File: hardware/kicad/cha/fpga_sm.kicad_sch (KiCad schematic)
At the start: 31 parts, among them J3 PROG SM, U15 iCE40HX4K-TQ144, U16 W25Q32JVSS, X2 25 MHz 3,3 V

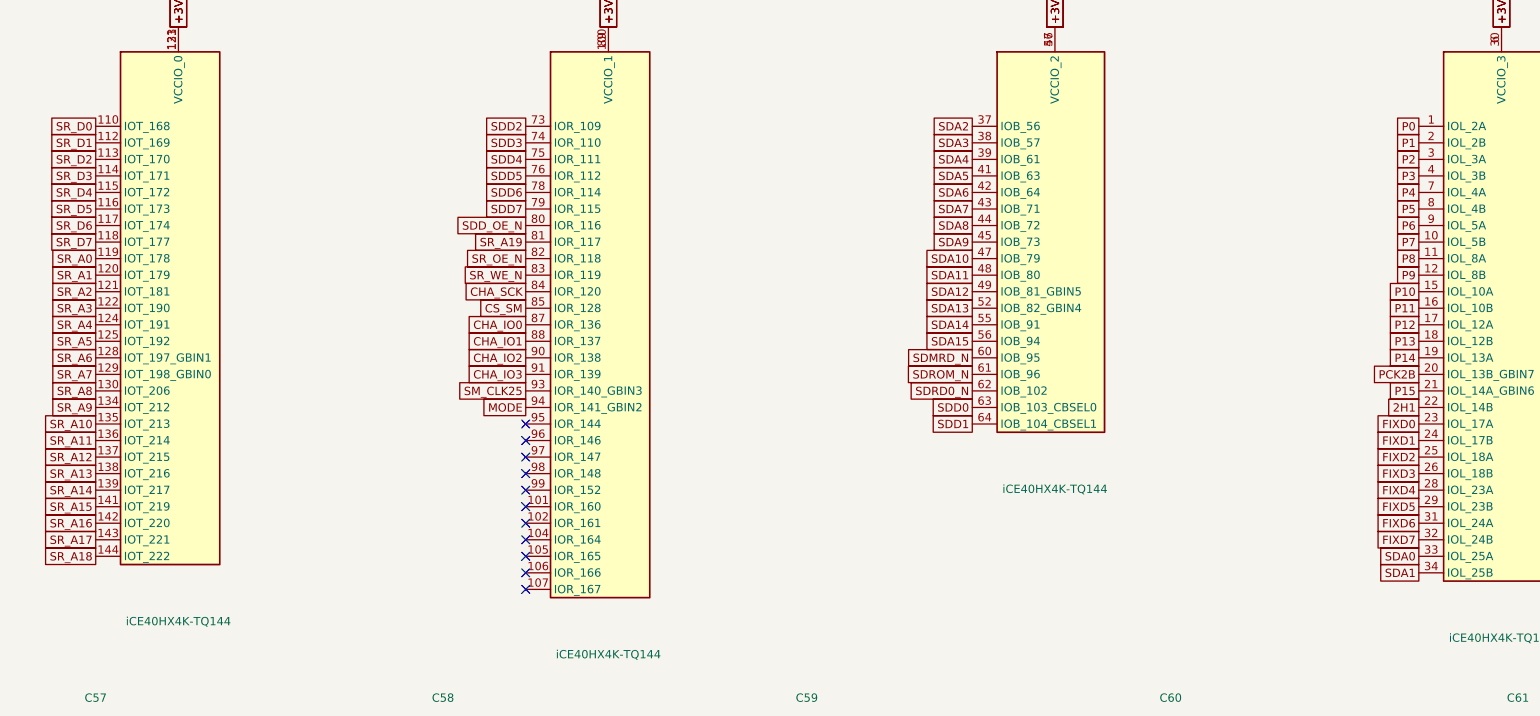
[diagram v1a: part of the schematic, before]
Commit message: Circuits imprimés 2 couches : placement et affectation des broches FPGA
- hardware/gen/pcb.py : empreintes et réseaux depuis boards.py, contour
  depuis outline.py ; ancres placées (contacts, rangée de tampons, FPGA,
  mémoires ; CHA : Pico au centre, microSD et bouton en haut), passifs
  au plus près de leur broche, masse coulée sur les deux faces.
- --pins : signaux des FPGA affectés aux broches tournées vers leur
  cible en conservant l'ordre circulaire (pins_opt.json, repris par
  fpga_pins.py) ; stable en trois passes.
- boards.py : canaux des tampons triés selon la position des contacts.
- hardware/gen/route.py : export Specctra, Freerouting, relecture de la
  session, DRC.
Placement-routage FPGA avec les nouvelles broches : en cours de
vérification.

Co-Authored-By: Claude Opus 5.5 <noreply@anthropic.com>
Claude-Session: https://claude.ai/code/session_01WKfXP1YJ8otGxZ5dsY6Agh
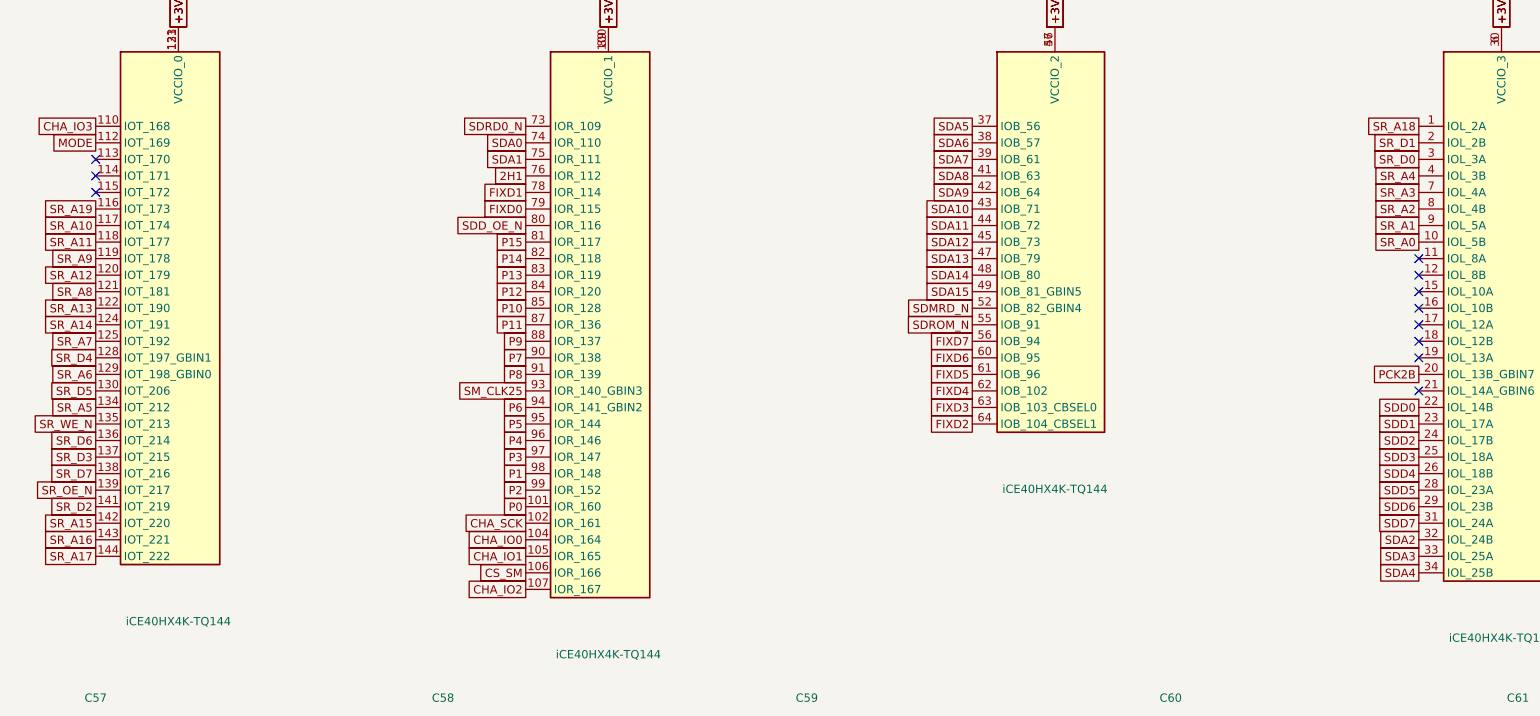
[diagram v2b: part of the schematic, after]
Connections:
- net 2H1: now also U15.76 (IOR_112); no longer U15.22 (IOL_14B)
- net CHA_IO0: now also U15.104 (IOR_164); no longer U15.87 (IOR_136)
- net CHA_IO1: now also U15.105 (IOR_165); no longer U15.88 (IOR_137)
- net CHA_IO2: now also U15.107 (IOR_167); no longer U15.90 (IOR_138)
- net CHA_IO3: now also U15.110 (IOT_168); no longer U15.91 (IOR_139)
- net CHA_SCK: now also U15.102 (IOR_161); no longer U15.84 (IOR_120)
- net CS_SM: now also U15.106 (IOR_166); no longer U15.85 (IOR_128)
- net FIXD0: now also U15.79 (IOR_115); no longer U15.23 (IOL_17A)
- net FIXD1: now also U15.78 (IOR_114); no longer U15.24 (IOL_17B)
- net FIXD2: now also U15.64 (IOB_104_CBSEL1); no longer U15.25 (IOL_18A)
- net FIXD3: now also U15.63 (IOB_103_CBSEL0); no longer U15.26 (IOL_18B)
- net FIXD4: now also U15.62 (IOB_102); no longer U15.28 (IOL_23A)
- net FIXD5: now also U15.61 (IOB_96); no longer U15.29 (IOL_23B)
- net FIXD6: now also U15.60 (IOB_95); no longer U15.31 (IOL_24A)
- net FIXD7: now also U15.56 (IOB_94); no longer U15.32 (IOL_24B)
- net MODE: now also U15.112 (IOT_169); no longer U15.94 (IOR_141_GBIN2)
- net P0: now also U15.101 (IOR_160); no longer U15.1 (IOL_2A)
- net P1: now also U15.98 (IOR_148); no longer U15.2 (IOL_2B)
- net P10: now also U15.85 (IOR_128); no longer U15.15 (IOL_10A)
- net P11: now also U15.87 (IOR_136); no longer U15.16 (IOL_10B)
- net P12: now also U15.84 (IOR_120); no longer U15.17 (IOL_12A)
- net P13: now also U15.83 (IOR_119); no longer U15.18 (IOL_12B)
- net P14: now also U15.82 (IOR_118); no longer U15.19 (IOL_13A)
- net P15: now also U15.81 (IOR_117); no longer U15.21 (IOL_14A_GBIN6)
- net P2: now also U15.99 (IOR_152); no longer U15.3 (IOL_3A)
- net P3: now also U15.97 (IOR_147); no longer U15.4 (IOL_3B)
- net P4: now also U15.96 (IOR_146); no longer U15.7 (IOL_4A)
- net P5: now also U15.95 (IOR_144); no longer U15.8 (IOL_4B)
- net P6: now also U15.94 (IOR_141_GBIN2); no longer U15.9 (IOL_5A)
- net P7: now also U15.90 (IOR_138); no longer U15.10 (IOL_5B)
- net P8: now also U15.91 (IOR_139); no longer U15.11 (IOL_8A)
- net P9: now also U15.88 (IOR_137); no longer U15.12 (IOL_8B)
- net SDA0: now also U15.74 (IOR_110); no longer U15.33 (IOL_25A)
- net SDA1: now also U15.75 (IOR_111); no longer U15.34 (IOL_25B)
- net SDA10: now also U15.43 (IOB_71); no longer U15.47 (IOB_79)
- net SDA11: now also U15.44 (IOB_72); no longer U15.48 (IOB_80)
- net SDA12: now also U15.45 (IOB_73); no longer U15.49 (IOB_81_GBIN5)
- net SDA13: now also U15.47 (IOB_79); no longer U15.52 (IOB_82_GBIN4)
- net SDA14: now also U15.48 (IOB_80); no longer U15.55 (IOB_91)
- net SDA15: now also U15.49 (IOB_81_GBIN5); no longer U15.56 (IOB_94)
- net SDA2: now also U15.32 (IOL_24B); no longer U15.37 (IOB_56)
- net SDA3: now also U15.33 (IOL_25A); no longer U15.38 (IOB_57)
- net SDA4: now also U15.34 (IOL_25B); no longer U15.39 (IOB_61)
- net SDA5: now also U15.37 (IOB_56); no longer U15.41 (IOB_63)
- net SDA6: now also U15.38 (IOB_57); no longer U15.42 (IOB_64)
- net SDA7: now also U15.39 (IOB_61); no longer U15.43 (IOB_71)
- net SDA8: now also U15.41 (IOB_63); no longer U15.44 (IOB_72)
- net SDA9: now also U15.42 (IOB_64); no longer U15.45 (IOB_73)
- net SDD0: now also U15.22 (IOL_14B); no longer U15.63 (IOB_103_CBSEL0)
- net SDD1: now also U15.23 (IOL_17A); no longer U15.64 (IOB_104_CBSEL1)
- net SDD2: now also U15.24 (IOL_17B); no longer U15.73 (IOR_109)
- net SDD3: now also U15.25 (IOL_18A); no longer U15.74 (IOR_110)
- net SDD4: now also U15.26 (IOL_18B); no longer U15.75 (IOR_111)
- net SDD5: now also U15.28 (IOL_23A); no longer U15.76 (IOR_112)
- net SDD6: now also U15.29 (IOL_23B); no longer U15.78 (IOR_114)
- net SDD7: now also U15.31 (IOL_24A); no longer U15.79 (IOR_115)
- net SDMRD_N: now also U15.52 (IOB_82_GBIN4); no longer U15.60 (IOB_95)
- net SDRD0_N: now also U15.73 (IOR_109); no longer U15.62 (IOB_102)
- net SDROM_N: now also U15.55 (IOB_91); no longer U15.61 (IOB_96)
- net SR_A0: now also U15.10 (IOL_5B); no longer U15.119 (IOT_178)
- net SR_A1: now also U15.9 (IOL_5A); no longer U15.120 (IOT_179)
- net SR_A10: now also U15.117 (IOT_174); no longer U15.135 (IOT_213)
- net SR_A11: now also U15.118 (IOT_177); no longer U15.136 (IOT_214)
- net SR_A12: now also U15.120 (IOT_179); no longer U15.137 (IOT_215)
- net SR_A13: now also U15.122 (IOT_190); no longer U15.138 (IOT_216)
- net SR_A14: now also U15.124 (IOT_191); no longer U15.139 (IOT_217)
- net SR_A15: now also U15.142 (IOT_220); no longer U15.141 (IOT_219)
- net SR_A16: now also U15.143 (IOT_221); no longer U15.142 (IOT_220)
- net SR_A17: now also U15.144 (IOT_222); no longer U15.143 (IOT_221)
- net SR_A18: now also U15.1 (IOL_2A); no longer U15.144 (IOT_222)
- net SR_A19: now also U15.116 (IOT_173); no longer U15.81 (IOR_117)
- net SR_A2: now also U15.8 (IOL_4B); no longer U15.121 (IOT_181)
- net SR_A3: now also U15.7 (IOL_4A); no longer U15.122 (IOT_190)
- net SR_A4: now also U15.4 (IOL_3B); no longer U15.124 (IOT_191)
- net SR_A5: now also U15.134 (IOT_212); no longer U15.125 (IOT_192)
- net SR_A6: now also U15.129 (IOT_198_GBIN0); no longer U15.128 (IOT_197_GBIN1)
- net SR_A7: now also U15.125 (IOT_192); no longer U15.129 (IOT_198_GBIN0)
- net SR_A8: now also U15.121 (IOT_181); no longer U15.130 (IOT_206)
- net SR_A9: now also U15.119 (IOT_178); no longer U15.134 (IOT_212)
- net SR_D0: now also U15.3 (IOL_3A); no longer U15.110 (IOT_168)
- net SR_D1: now also U15.2 (IOL_2B); no longer U15.112 (IOT_169)
- net SR_D2: now also U15.141 (IOT_219); no longer U15.113 (IOT_170)
- net SR_D3: now also U15.137 (IOT_215); no longer U15.114 (IOT_171)
- net SR_D4: now also U15.128 (IOT_197_GBIN1); no longer U15.115 (IOT_172)
- net SR_D5: now also U15.130 (IOT_206); no longer U15.116 (IOT_173)
- net SR_D6: now also U15.136 (IOT_214); no longer U15.117 (IOT_174)
- net SR_D7: now also U15.138 (IOT_216); no longer U15.118 (IOT_177)
- net SR_OE_N: now also U15.139 (IOT_217); no longer U15.82 (IOR_118)
- net SR_WE_N: now also U15.135 (IOT_213); no longer U15.83 (IOR_119)

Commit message: FPGA configurés par le RP2350 depuis la carte SD (plus de flash)
- Matériel : flash SPI retirées (4 W25Q32, 12 résistances, 4
  condensateurs). Le bus de liaison arrive sur les broches de
  configuration des iCE40 (LK_SCK -> 70 SCK, LK_IO[0] -> 68 SDI,
  LK_CS_N -> 71 SS), qui redeviennent ces entrées après le démarrage.
  CRESET_N commun aux 4 FPGA, tiré à la masse, piloté par le RP2350
  (GP28) ; câble PROG-CHA en 2 x 7 (CRESET_N + masse). Connecteur 2 x 3
  de secours par FPGA (iceprog -S).
- Firmware : fpga_boot.c (reset commun en mode SPI esclave, envoi des
  SDAES/fpga_*.bin l'un après l'autre, contrôle de CDONE) ; testé sur
  PC (bitstreams reçus à l'identique, FPGA laissés en reset si un
  fichier manque).
- make -C hdl sd : fichiers à copier sur la carte SD.
- PCB : table de placement et références des FPGA mises à jour,
  broches réoptimisées.
Placement-routage des FPGA avec les nouvelles broches : en cours.

Co-Authored-By: Claude Opus 5.5 <noreply@anthropic.com>
Claude-Session: https://claude.ai/code/session_01WKfXP1YJ8otGxZ5dsY6Agh
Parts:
- removed C70, C71: 100n, Capacitor_SMD:C_0603_1608Metric, symbol Device:C
- removed R13, R14: 100, Resistor_SMD:R_0603_1608Metric, symbol Device:R
- removed R15, R16, R17, R18: 10k, Resistor_SMD:R_0603_1608Metric, symbol Device:R
- removed U15: iCE40HX4K-TQ144, Package_QFP:TQFP-144_20x20mm_P0.5mm, symbol FPGA_Lattice:ICE40HX4K-TQ144
- removed U16: W25Q32JVSS, Package_SO:SOIC-8_5.23x5.23mm_P1.27mm, symbol Memory_Flash:W25Q32JVSS
- added C50: 100n, Capacitor_SMD:C_0603_1608Metric, symbol Device:C
- added R10, R11: 100, Resistor_SMD:R_0603_1608Metric, symbol Device:R
- added R12: 10k, Resistor_SMD:R_0603_1608Metric, symbol Device:R
- added U14: iCE40HX4K-TQ144, Package_QFP:TQFP-144_20x20mm_P0.5mm, symbol FPGA_Lattice:ICE40HX4K-TQ144
- C54, C64, C67: value 100n -> 10u; footprint Capacitor_SMD:C_0603_1608Metric -> Capacitor_SMD:C_0805_2012Metric
- C55, C66, C68: value 10u -> 100n; footprint Capacitor_SMD:C_0805_2012Metric -> Capacitor_SMD:C_0603_1608Metric
- J3: value PROG SM -> CONF SM
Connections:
- net SM_FL_CS_N is gone; now on net CS_SM: J3.2 (Pin_2)
- net SM_FL_DO is gone; now on net CHA_IO0: J3.4 (Pin_4)
- net SM_FL_SCK is gone; now on net CHA_SCK: J3.1 (Pin_1)
- net +1V2: now also C50.1, R10.1, R11.1, U14.111 (VCC), U14.27 (VCC), U14.40 (VCC), U14.92 (VCC); no longer C55.1
- net +3V3: now also C55.1, C69.1, U14.100 (VCCIO_1), U14.108 (VPP_2V5), U14.123 (VCCIO_0), U14.131 (VCCIO_0), U14.30 (VCCIO_3), U14.46 (VCCIO_2), U14.57 (VCCIO_2), U14.6 (VCCIO_3), U14.72 (VCC_SPI), U14.89 (VCCIO_1); no longer C65.1
- net 2H1: now also U14.78 (IOR_114)
- net CDONE: now also U14.65 (CDONE)
- net CHA_IO0: now also U14.68 (IOB_106_SDI)
- net CHA_IO1: now also U14.104 (IOR_164)
- net CHA_IO2: now also U14.105 (IOR_165)
- net CHA_IO3: now also U14.106 (IOR_166)
- net CHA_SCK: now also U14.70 (IOB_107_SCK)
- net CS_SM: now also U14.71 (IOB_108_SS)
- net FIXD0: now also U14.80 (IOR_116)
- net FIXD1: now also U14.79 (IOR_115)
- net FIXD2: now also U14.73 (IOR_109)
- net FIXD3: now also U14.64 (IOB_104_CBSEL1)
- net FIXD4: now also U14.63 (IOB_103_CBSEL0)
- net FIXD5: now also U14.62 (IOB_102)
- net FIXD6: now also U14.61 (IOB_96)
- net FIXD7: now also U14.60 (IOB_95)
- net GND: now also C50.2, R12.2, U14.103 (GND), U14.127 (GNDPLL1), U14.13 (GND), U14.132 (GND), U14.14 (GND), U14.140 (GND), U14.5 (GND), U14.53 (GNDPLL0), U14.59 (GND), U14.69 (GND), U14.86 (GND)
- net MODE: now also U14.107 (IOR_167)
- net P0: now also U14.102 (IOR_161)
- net P1: now also U14.99 (IOR_152)
- net P10: now also U14.85 (IOR_128)
- net P11: now also U14.87 (IOR_136)
- net P12: now also U14.88 (IOR_137)
- net P13: now also U14.84 (IOR_120)
- net P14: now also U14.83 (IOR_119)
- net P15: now also U14.82 (IOR_118)
- net P2: now also U14.101 (IOR_160)
- net P3: now also U14.98 (IOR_148)
- net P4: now also U14.97 (IOR_147)
- net P5: now also U14.96 (IOR_146)
- net P6: now also U14.95 (IOR_144)
- net P7: now also U14.91 (IOR_139)
- net P8: now also U14.94 (IOR_141_GBIN2)
- net P9: now also U14.90 (IOR_138)
- net PCK2B: now also U14.20 (IOL_13B_GBIN7)
- net SDA0: now also U14.75 (IOR_111)
- net SDA1: now also U14.76 (IOR_112)
- net SDA10: now also U14.44 (IOB_72)
- net SDA11: now also U14.45 (IOB_73)
- net SDA12: now also U14.47 (IOB_79)
- net SDA13: now also U14.48 (IOB_80)
- net SDA14: now also U14.49 (IOB_81_GBIN5)
- net SDA15: now also U14.52 (IOB_82_GBIN4)
- net SDA2: now also U14.33 (IOL_25A)
- net SDA3: now also U14.34 (IOL_25B)
- net SDA4: now also U14.37 (IOB_56)
- net SDA5: now also U14.38 (IOB_57)
- net SDA6: now also U14.39 (IOB_61)
- net SDA7: now also U14.41 (IOB_63)
- net SDA8: now also U14.42 (IOB_64)
- net SDA9: now also U14.43 (IOB_71)
- net SDD0: now also U14.23 (IOL_17A)
- net SDD1: now also U14.24 (IOL_17B)
- net SDD2: now also U14.25 (IOL_18A)
- net SDD3: now also U14.26 (IOL_18B)
- net SDD4: now also U14.28 (IOL_23A)
- net SDD5: now also U14.29 (IOL_23B)
- net SDD6: now also U14.31 (IOL_24A)
- net SDD7: now also U14.32 (IOL_24B)
- net SDD_OE_N: now also U14.81 (IOR_117)
- net SDMRD_N: now also U14.55 (IOB_91)
- net SDRD0_N: now also U14.74 (IOR_110)
- net SDROM_N: now also U14.56 (IOB_94)
- net SM_CLK25: now also U14.93 (IOR_140_GBIN3)
- net SM_VCCPLL0: now also C65.1, R10.2, U14.54 (VCCPLL0); no longer C67.1
- net SM_VCCPLL1: now also C67.1, R11.2, U14.126 (VCCPLL1); no longer C69.1
- net SR_A0: now also U14.10 (IOL_5B)
- net SR_A1: now also U14.9 (IOL_5A)
- net SR_A10: now also U14.117 (IOT_174)
- net SR_A11: now also U14.118 (IOT_177)
- net SR_A12: now also U14.120 (IOT_179)
- net SR_A13: now also U14.122 (IOT_190)
- net SR_A14: now also U14.124 (IOT_191)
- net SR_A15: now also U14.142 (IOT_220)
- net SR_A16: now also U14.143 (IOT_221)
- net SR_A17: now also U14.144 (IOT_222)
- net SR_A18: now also U14.1 (IOL_2A)
- net SR_A19: now also U14.116 (IOT_173)
- net SR_A2: now also U14.8 (IOL_4B)
- net SR_A3: now also U14.7 (IOL_4A)
- net SR_A4: now also U14.4 (IOL_3B)
- net SR_A5: now also U14.134 (IOT_212)
- net SR_A6: now also U14.129 (IOT_198_GBIN0)
- net SR_A7: now also U14.125 (IOT_192)
- net SR_A8: now also U14.121 (IOT_181)
- net SR_A9: now also U14.119 (IOT_178)
- net SR_D0: now also U14.3 (IOL_3A)
- net SR_D1: now also U14.2 (IOL_2B)
- net SR_D2: now also U14.141 (IOT_219)
- net SR_D3: now also U14.137 (IOT_215)
- net SR_D4: now also U14.128 (IOT_197_GBIN1)
- net SR_D5: now also U14.130 (IOT_206)
- net SR_D6: now also U14.136 (IOT_214)
- net SR_D7: now also U14.138 (IOT_216)
- net SR_OE_N: now also U14.139 (IOT_217)
- net SR_WE_N: now also U14.135 (IOT_213)
- net SM_CRESET_N renamed CRESET_N
- net CRESET_N: now also R12.1, U14.66 (~{CRESET})
- net SM_FL_DI renamed SM_SDO
- net SM_SDO: now also U14.67 (IOB_105_SDO)
- no-connect marks 19 -> 22
